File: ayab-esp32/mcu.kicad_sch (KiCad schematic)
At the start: 27 parts, among them J201 SPARE1, J202 SPARE0, Q201 AO3400A, SW201 USER, SW202 RESET, SW203 BOOTSEL, U201 ESP32-S3-MINI-1

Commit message: Route ESP32 native USB to GPIO19/20 [skip ci]
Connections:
- net BUZZER: now also U201.23 (GPIO19/U1RTS/ADC2_CH8/CLK_OUT2/USB_D-); no longer U201.34 (GPIO38/FSPIWP/SUBSPIWP)
- net USB_M: now also U201.34 (GPIO38/FSPIWP/SUBSPIWP); no longer U201.23 (GPIO19/U1RTS/ADC2_CH8/CLK_OUT2/USB_D-)
- net USB_P: now also U201.41 (GPIO45); no longer U201.24 (GPIO20/U1CTS/ADC2_CH9/CLK_OUT1/USB_D+)
- net VCC_SPI: no longer U201.41 (GPIO45)
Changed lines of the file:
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@@
     (stroke (width 0) (type default))
   )
-  (wire (pts (xy 185.42 120.65) (xy 198.12 120.65))
-    (stroke (width 0) (type default))
-  )
   (wire (pts (xy 41.91 115.57) (xy 41.91 125.73))
     (stroke (width 0) (type default))
@@
     (stroke (width 0) (type default))
   )
-  (wire (pts (xy 185.42 64.77) (xy 198.12 64.77))
+  (wire (pts (xy 185.42 120.65) (xy 198.12 120.65))
     (stroke (width 0) (type default))
   )
@@
     (stroke (width 0) (type default))
   )
-  (wire (pts (xy 185.42 118.11) (xy 198.12 118.11))
+  (wire (pts (xy 185.42 67.31) (xy 198.12 67.31))
     (stroke (width 0) (type default))
   )
@@
     (stroke (width 0) (type default))
   )
-  (wire (pts (xy 185.42 67.31) (xy 198.12 67.31))
+  (wire (pts (xy 185.42 118.11) (xy 198.12 118.11))
     (stroke (width 0) (type default))
   )
@@
     (effects (font (size 1.27 1.27)) (justify left bottom))
   )
-  (label "BUZZER" (at 198.12 118.11 180) (fields_autoplaced)
+  (label "BUZZER" (at 198.12 67.31 180) (fields_autoplaced)
     (effects (font (size 1.27 1.27)) (justify right bottom))
   )
@@
     (effects (font (size 1.27 1.27)) (justify left bottom))
   )
-  (label "VCC_SPI" (at 198.12 120.65 180) (fields_autoplaced)
-    (effects (font (size 1.27 1.27)) (justify right bottom))
-  )
-  (label "ESP14" (at 198.12 107.95 180) (fields_autoplaced)
+    (label "ESP14" (at 198.12 107.95 180) (fields_autoplaced)
     (effects (font (size 1.27 1.27)) (justify right bottom))
   )
@@
     (effects (font (size 1.27 1.27)) (justify left))
   )
-  (hierarchical_label "USB_M" (shape bidirectional) (at 198.12 67.31 0) (fields_autoplaced)
+  (hierarchical_label "USB_M" (shape bidirectional) (at 198.12 118.11 0) (fields_autoplaced)
     (effects (font (size 1.27 1.27)) (justify left))
   )
@@
     (effects (font (size 1.27 1.27)) (justify left))
   )
-  (hierarchical_label "USB_P" (shape bidirectional) (at 198.12 64.77 0) (fields_autoplaced)
+  (hierarchical_label "USB_P" (shape bidirectional) (at 198.12 120.65 0) (fields_autoplaced)
     (effects (font (size 1.27 1.27)) (justify left))
   )

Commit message: Route ESP32 native USB to GPIO19/20
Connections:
- net BUZZER: now also U201.34 (GPIO38/FSPIWP/SUBSPIWP); no longer U201.23 (GPIO19/U1RTS/ADC2_CH8/CLK_OUT2/USB_D-)
- net USB_M: now also U201.23 (GPIO19/U1RTS/ADC2_CH8/CLK_OUT2/USB_D-); no longer U201.34 (GPIO38/FSPIWP/SUBSPIWP)
- net USB_P: now also U201.24 (GPIO20/U1CTS/ADC2_CH9/CLK_OUT1/USB_D+); no longer U201.41 (GPIO45)
- net VCC_SPI: now also U201.41 (GPIO45)
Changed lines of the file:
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@@
     (stroke (width 0) (type default))
   )
-  (wire (pts (xy 185.42 120.65) (xy 198.12 120.65))
+  (wire (pts (xy 185.42 64.77) (xy 198.12 64.77))
     (stroke (width 0) (type default))
   )
@@
     (stroke (width 0) (type default))
   )
-  (wire (pts (xy 185.42 67.31) (xy 198.12 67.31))
+  (wire (pts (xy 185.42 120.65) (xy 198.12 120.65))
+    (stroke (width 0) (type default))
+  )
+  (wire (pts (xy 185.42 118.11) (xy 198.12 118.11))
     (stroke (width 0) (type default))
   )
@@
     (stroke (width 0) (type default))
   )
-  (wire (pts (xy 185.42 118.11) (xy 198.12 118.11))
+  (wire (pts (xy 185.42 67.31) (xy 198.12 67.31))
     (stroke (width 0) (type default))
   )
@@
     (effects (font (size 1.27 1.27)) (justify left bottom))
   )
-  (label "BUZZER" (at 198.12 67.31 180) (fields_autoplaced)
+  (label "BUZZER" (at 198.12 118.11 180) (fields_autoplaced)
     (effects (font (size 1.27 1.27)) (justify right bottom))
   )
@@
     (effects (font (size 1.27 1.27)) (justify left bottom))
   )
-    (label "ESP14" (at 198.12 107.95 180) (fields_autoplaced)
+    (label "VCC_SPI" (at 198.12 120.65 180) (fields_autoplaced)
+    (effects (font (size 1.27 1.27)) (justify right bottom))
+  )
+  (label "ESP14" (at 198.12 107.95 180) (fields_autoplaced)
     (effects (font (size 1.27 1.27)) (justify right bottom))
   )
@@
     (effects (font (size 1.27 1.27)) (justify left))
   )
-  (hierarchical_label "USB_M" (shape bidirectional) (at 198.12 118.11 0) (fields_autoplaced)
+  (hierarchical_label "USB_M" (shape bidirectional) (at 198.12 67.31 0) (fields_autoplaced)
     (effects (font (size 1.27 1.27)) (justify left))
   )
@@
     (effects (font (size 1.27 1.27)) (justify left))
   )
-  (hierarchical_label "USB_P" (shape bidirectional) (at 198.12 120.65 0) (fields_autoplaced)
+  (hierarchical_label "USB_P" (shape bidirectional) (at 198.12 64.77 0) (fields_autoplaced)
     (effects (font (size 1.27 1.27)) (justify left))
   )

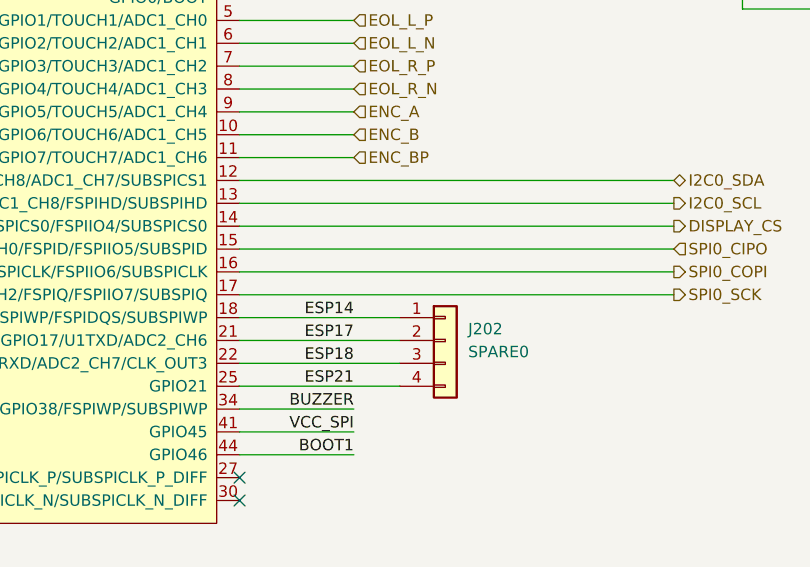
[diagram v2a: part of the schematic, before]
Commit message: Bypass KH910 K-L comparators and add pull-ups
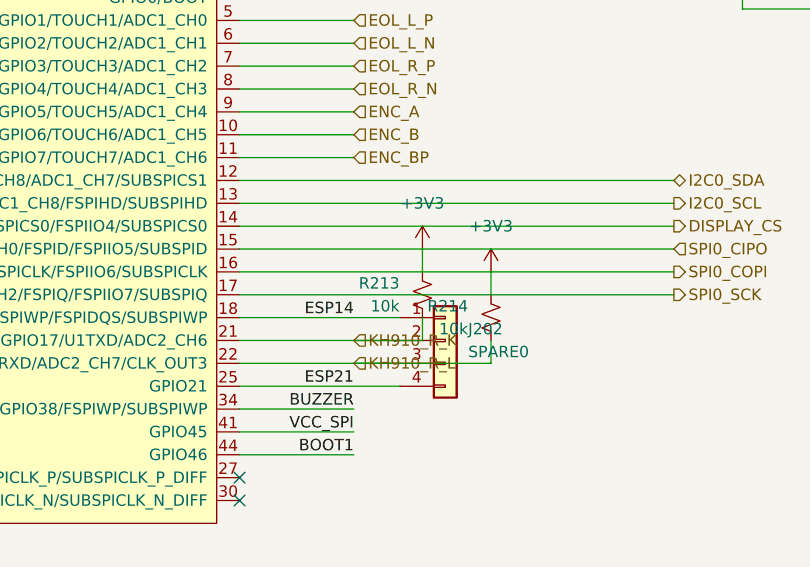
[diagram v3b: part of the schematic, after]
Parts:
- added R213, R214: 10k, Resistor_SMD:R_0603_1608Metric, symbol ayab-lib:R_Small_US
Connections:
- net +3V3: now also R213.1, R214.1
- net ESP17 renamed KH910_R_K
- net KH910_R_K: now also R213.2
- net ESP18 renamed KH910_R_L
- net KH910_R_L: now also R214.2
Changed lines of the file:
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@@
     (effects (font (size 1.27 1.27)) (justify left bottom))
+  )
+  (wire (pts (xy 198.12 110.49) (xy 205.74 110.49))
+    (stroke (width 0) (type default))
+  )
+  (wire (pts (xy 205.74 110.49) (xy 205.74 107.95))
+    (stroke (width 0) (type default))
+  )
+  (wire (pts (xy 205.74 102.87) (xy 205.74 100.33))
+    (stroke (width 0) (type default))
+  )
+  (wire (pts (xy 198.12 113.03) (xy 213.36 113.03))
+    (stroke (width 0) (type default))
+  )
+  (wire (pts (xy 213.36 113.03) (xy 213.36 110.49))
+    (stroke (width 0) (type default))
+  )
+  (wire (pts (xy 213.36 105.41) (xy 213.36 102.87))
+    (stroke (width 0) (type default))
   )
   (label "VCC_SPI" (at 132.08 173.99 0) (fields_autoplaced)
@@
     (effects (font (size 1.27 1.27)) (justify right bottom))
   )
-  (label "ESP18" (at 198.12 113.03 180) (fields_autoplaced)
-    (effects (font (size 1.27 1.27)) (justify right bottom))
-  )
-  (label "GRN" (at 85.09 120.65 0) (fields_autoplaced)
+    (label "GRN" (at 85.09 120.65 0) (fields_autoplaced)
     (effects (font (size 1.27 1.27)) (justify left bottom))
   )
@@
     (effects (font (size 1.27 1.27)) (justify left bottom))
   )
-  (label "ESP17" (at 198.12 110.49 180) (fields_autoplaced)
-    (effects (font (size 1.27 1.27)) (justify right bottom))
-  )
-  (label "nRST" (at 87.63 57.15 0) (fields_autoplaced)
+    (label "nRST" (at 87.63 57.15 0) (fields_autoplaced)
     (effects (font (size 1.27 1.27)) (justify left bottom))
   )
@@
   (label "ESP21" (at 198.12 115.57 180) (fields_autoplaced)
     (effects (font (size 1.27 1.27)) (justify right bottom))
+  )
+  (hierarchical_label "KH910_R_L" (shape input) (at 198.12 113.03 0) (fields_autoplaced)
+    (effects (font (size 1.27 1.27)) (justify left))
+  )
+  (hierarchical_label "KH910_R_K" (shape input) (at 198.12 110.49 0) (fields_autoplaced)
+    (effects (font (size 1.27 1.27)) (justify left))
   )
   (hierarchical_label "SPI0_COPI" (shape output) (at 233.68 102.87 0) (fields_autoplaced)
@@
         )
       )
+    )
+  )
+(symbol (lib_id "ayab-lib:R_Small_US") (at 205.74 105.41 0) (unit 1)
+    (in_bom yes) (on_board yes) (dnp no)
+    (property "Reference" "R213" (at 203.2 104.14 0)
+      (effects (font (size 1.27 1.27)) (justify right))
+    )
+    (property "Value" "10k" (at 203.2 106.68 0)
+      (effects (font (size 1.27 1.27)) (justify right))
+    )
+    (property "Footprint" "Resistor_SMD:R_0603_1608Metric" (at 205.74 105.41 0)
+      (effects (font (size 1.27 1.27)) hide)
+    )
+    (property "Datasheet" "~" (at 205.74 105.41 0)
+      (effects (font (size 1.27 1.27)) hide)
+    )
+    (property "LCSC ID" "C25804" (at 205.74 105.41 0)
+      (effects (font (size 1.27 1.27)) hide)
+    )
+    (property "Voltage rating" "" (at 205.74 105.41 0)
+      (effects (font (size 1.27 1.27)) hide)
+    )
+    (property "Package" "0603" (at 205.74 105.41 0)
+      (effects (font (size 1.27 1.27)) hide)
+    )
+    (property "OEM PN" "0603WAF1002T5E" (at 205.74 105.41 0)
+      (effects (font (size 1.27 1.27)) hide)
+    )
+    (property "OEM" "UNI-ROYAL(Uniroyal Elec)" (at 205.74 105.41 0)
+      (effects (font (size 1.27 1.27)) hide)
+    )
+    (pin "1")
+    (pin "2")
+    (instances
+      (project "ayab-esp32"
+        (path "/ad16b75f-afc8-4717-a7c6-8dd7b69a18e2/a7e0db0f-e473-44d4-a2fe-681f732aacb2"
+          (reference "R213") (unit 1)
+        )
+      )
+    )
+  )
+(symbol (lib_id "ayab-lib:R_Small_US") (at 213.36 107.95 0) (unit 1)
+    (in_bom yes) (on_board yes) (dnp no)
+    (property "Reference" "R214" (at 210.82 106.68 0)
+      (effects (font (size 1.27 1.27)) (justify right))
+    )
+    (property "Value" "10k" (at 210.82 109.22 0)
+      (effects (font (size 1.27 1.27)) (justify right))
+    )
+    (property "Footprint" "Resistor_SMD:R_0603_1608Metric" (at 213.36 107.95 0)
+      (effects (font (size 1.27 1.27)) hide)
+    )
+    (property "Datasheet" "~" (at 213.36 107.95 0)
+      (effects (font (size 1.27 1.27)) hide)
+    )
+    (property "LCSC ID" "C25804" (at 213.36 107.95 0)
+      (effects (font (size 1.27 1.27)) hide)
+    )
+    (property "Voltage rating" "" (at 213.36 107.95 0)
+      (effects (font (size 1.27 1.27)) hide)
+    )
+    (property "Package" "0603" (at 213.36 107.95 0)
+      (effects (font (size 1.27 1.27)) hide)
+    )
+    (property "OEM PN" "0603WAF1002T5E" (at 213.36 107.95 0)
+      (effects (font (size 1.27 1.27)) hide)
+    )
+    (property "OEM" "UNI-ROYAL(Uniroyal Elec)" (at 213.36 107.95 0)
+      (effects (font (size 1.27 1.27)) hide)
+    )
+    (pin "1")
+    (pin "2")
+    (instances
+      (project "ayab-esp32"
+        (path "/ad16b75f-afc8-4717-a7c6-8dd7b69a18e2/a7e0db0f-e473-44d4-a2fe-681f732aacb2"
+          (reference "R214") (unit 1)
+        )
+      )
+    )
+  )
+(symbol (lib_id "power:+3V3") (at 205.74 100.33 0) (unit 1)
+    (in_bom yes) (on_board yes) (dnp no) (fields_autoplaced)
+    (property "Reference" "#PWR220" (at 205.74 104.14 0)
+      (effects (font (size 1.27 1.27)) hide)
+    )
+    (property "Value" "+3V3" (at 205.74 95.25 0)
+      (effects (font (size 1.27 1.27)))
+    )
+    (property "Footprint" "" (at 205.74 100.33 0)
+      (effects (font (size 1.27 1.27)) hide)
+    )
+    (property "Datasheet" "" (at 205.74 100.33 0)
+      (effects (font (size 1.27 1.27)) hide)
+    )
+    (pin "1")
+    (instances
+      (project "ayab-esp32"
+        (path "/ad16b75f-afc8-4717-a7c6-8dd7b69a18e2/a7e0db0f-e473-44d4-a2fe-681f732aacb2"
+          (reference "#PWR220") (unit 1)
+        )
+      )
+    )
+  )
+(symbol (lib_id "power:+3V3") (at 213.36 102.87 0) (unit 1)
+    (in_bom yes) (on_board yes) (dnp no) (fields_autoplaced)
+    (property "Reference" "#PWR221" (at 213.36 106.68 0)
+      (effects (font (size 1.27 1.27)) hide)
+    )
+    (property "Value" "+3V3" (at 213.36 97.79 0)
+      (effects (font (size 1.27 1.27)))
+    )
+    (property "Footprint" "" (at 213.36 102.87 0)
+      (effects (font (size 1.27 1.27)) hide)
+    )
+    (property "Datasheet" "" (at 213.36 102.87 0)
+      (effects (font (size 1.27 1.27)) hide)
+    )
+    (pin "1")
+    (instances
+      (project "ayab-esp32"
+        (path "/ad16b75f-afc8-4717-a7c6-8dd7b69a18e2/a7e0db0f-e473-44d4-a2fe-681f732aacb2"
+          (reference "#PWR221") (unit 1)
+        )
+      )

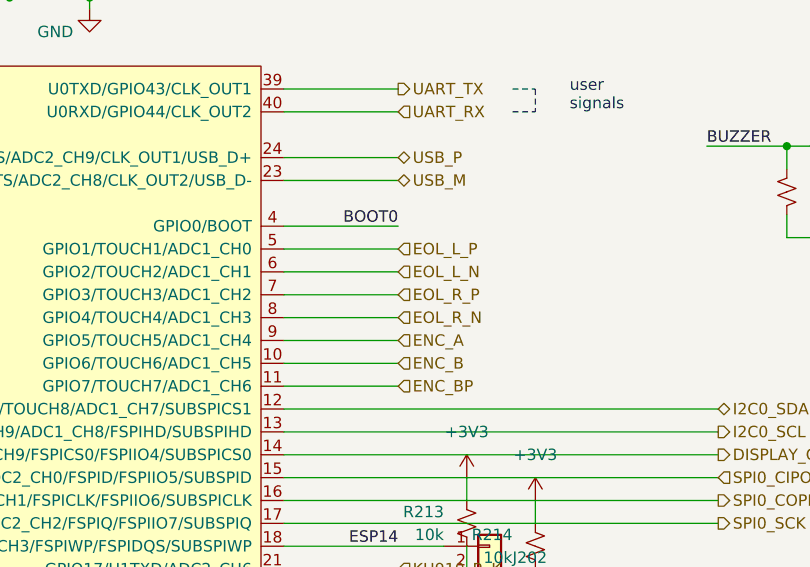
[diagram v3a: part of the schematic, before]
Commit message: Add passive analog Hall ADC paths
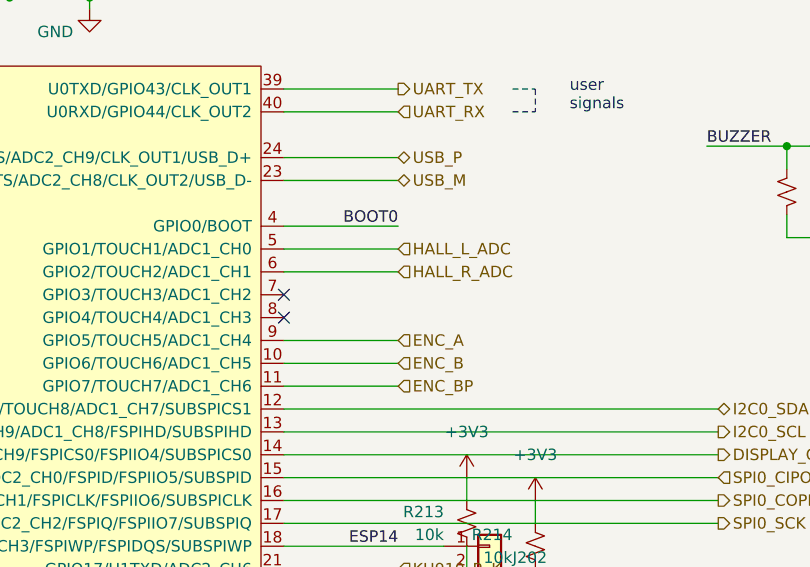
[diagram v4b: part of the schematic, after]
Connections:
- net EOL_L_N renamed HALL_R_ADC
- net EOL_L_P renamed HALL_L_ADC
- net EOL_R_N: no longer names the net of U201.8 (GPIO4/TOUCH4/ADC1_CH3)
- net EOL_R_P: no longer names the net of U201.7 (GPIO3/TOUCH3/ADC1_CH2)
- no-connect marks 6 -> 8
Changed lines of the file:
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@@
   (junction (at 41.91 99.06) (diameter 0) (color 0 0 0 0)
   )
+  (no_connect (at 185.42 82.55))
+  (no_connect (at 185.42 80.01))
   (no_connect (at 93.98 128.27))
   (no_connect (at 185.42 125.73))
@@
   (wire (pts (xy 185.42 77.47) (xy 198.12 77.47))
     (stroke (width 0) (type default))
-  )
-  (wire (pts (xy 198.12 82.55) (xy 185.42 82.55))
-    (stroke (width 0) (type default))
-  )
-  (wire (pts (xy 78.74 54.61) (xy 78.74 55.88))
+  )  (wire (pts (xy 78.74 54.61) (xy 78.74 55.88))
     (stroke (width 0) (type default))
   )
@@
   (wire (pts (xy 71.12 50.8) (xy 71.12 54.61))
     (stroke (width 0) (type default))
-  )
-  (wire (pts (xy 198.12 80.01) (xy 185.42 80.01))
-    (stroke (width 0) (type default))
-  )
-  (wire (pts (xy 185.42 113.03) (xy 203.2 113.03))
+  )  (wire (pts (xy 185.42 113.03) (xy 203.2 113.03))
     (stroke (width 0) (type default))
   )
@@
     (effects (font (size 1.27 1.27)) (justify left))
   )
-  (hierarchical_label "EOL_L_N" (shape input) (at 198.12 77.47 0) (fields_autoplaced)
-    (effects (font (size 1.27 1.27)) (justify left))
-  )
-  (hierarchical_label "EOL_R_N" (shape input) (at 198.12 82.55 0) (fields_autoplaced)
+  (hierarchical_label "HALL_R_ADC" (shape input) (at 198.12 77.47 0) (fields_autoplaced)
     (effects (font (size 1.27 1.27)) (justify left))
   )
-  (hierarchical_label "UART_RX" (shape input) (at 198.12 59.69 0) (fields_autoplaced)
+    (hierarchical_label "UART_RX" (shape input) (at 198.12 59.69 0) (fields_autoplaced)
     (effects (font (size 1.27 1.27)) (justify left))
   )
@@
     (effects (font (size 1.27 1.27)) (justify right))
   )
-  (hierarchical_label "EOL_L_P" (shape input) (at 198.12 74.93 0) (fields_autoplaced)
+  (hierarchical_label "HALL_L_ADC" (shape input) (at 198.12 74.93 0) (fields_autoplaced)
     (effects (font (size 1.27 1.27)) (justify left))
   )
@@
     (effects (font (size 1.27 1.27)) (justify right))
   )
-  (hierarchical_label "EOL_R_P" (shape input) (at 198.12 80.01 0) (fields_autoplaced)
-    (effects (font (size 1.27 1.27)) (justify left))
-  )
-  (hierarchical_label "USB_P" (shape bidirectional) (at 198.12 64.77 0) (fields_autoplaced)
+    (hierarchical_label "USB_P" (shape bidirectional) (at 198.12 64.77 0) (fields_autoplaced)
     (effects (font (size 1.27 1.27)) (justify left))
   )
